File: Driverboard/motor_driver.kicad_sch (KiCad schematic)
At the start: 21 parts

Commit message: WIP
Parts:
- removed R?: 47, symbol Device:R_Small
- R?: value 68 -> 39k
- R?: value 330 -> 27k
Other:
- note added: "The peak current of the motor is 9.5A and the peak phase current of the driver is 8A. The motor have 3 phases and at least two of them active at once. This means that the approximate minimum peak phase current needed for efficient control is: Ioutx = 9.5A / sqrt(3) ~ 5.48A. Therefore if cycle-by-cycle threshold is set to 6A > Ioutx it will be sufficient for the driver to handle the motor load. Th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"
- note added: "~1.35V"
- note removed: "1.25V ILIM gives 8A peak current limit."
- note removed: "~1.24V"
- moved on the sheet: C?, C_AVDD1, C_CP, C_FLY, C_VM1, C_VM2, IC?, L?, R?

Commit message: Powerboard v0.1, not ready for manufacturing yet
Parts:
- removed L? (x2): ?, symbol Device:L_Small
- R?: value 39k -> 27k
- R?: value 27k -> 20k
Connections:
- net GNDREF is gone; now on net GND: C?.2, C?.2, C_AVDD1.2, C_VM1.2, C_VM2.2, IC?.12 (PGND_1), IC?.15 (PGND_2), IC?.18 (PGND_3), IC?.2 (AGND_1), IC?.26 (AGND_2), IC?.4 (GND_BK), IC?.41 (EP), J?.8 (Pin_8), R?.2
- net VM is gone; now on net VCC: C_CP.2, C_VM1.1, C_VM2.1, IC?.10 (VM_2), IC?.11 (VM_3), IC?.9 (VM_1)
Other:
- note added: "The peak current of the motor is 9.5A and the peak phase current of the driver is 8A. The motor have 3 phases and at least two of them active at once. This means that the approximate minimum peak phase current needed for efficient control is: Ioutx = 9.5A / sqrt(3) ~ 5.48A. Therefore if cycle-by-cycle threshold is set to 5.48A*0.9 > Ilim it will be sufficient for the driver to handle the motor lo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"
- note added: "~1.40V"
- note removed: "The peak current of the motor is 9.5A and the peak phase current of the driver is 8A. The motor have 3 phases and at least two of them active at once. This means that the approximate minimum peak phase current needed for efficient control is: Ioutx = 9.5A / sqrt(3) ~ 5.48A. Therefore if cycle-by-cycle threshold is set to 6A > Ioutx it will be sufficient for the driver to handle the motor load. Th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"
- note removed: "~1.35V"

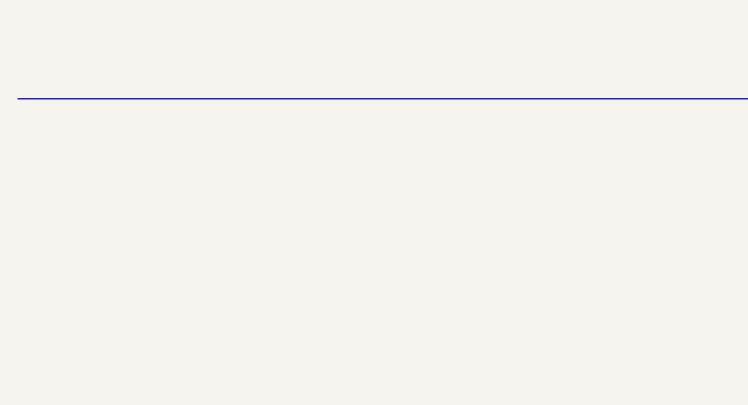
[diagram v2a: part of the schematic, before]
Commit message: DriverboardComp is the complete design, need to be evaluated
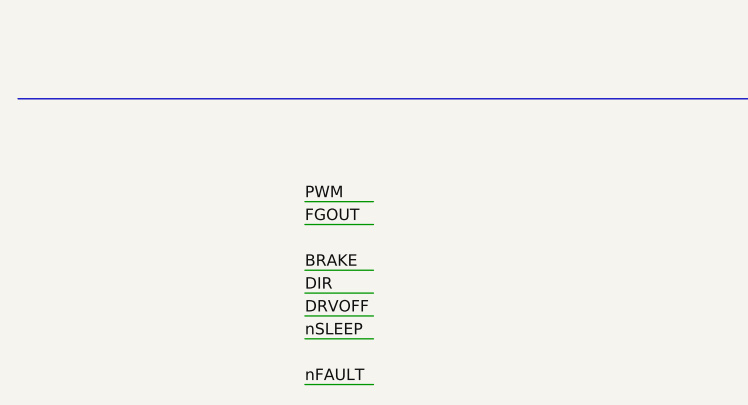
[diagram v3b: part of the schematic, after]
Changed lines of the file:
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@@
+    (stroke (width 0) (type default))
+  )
+  (wire (pts (xy 43.18 149.86) (xy 50.8 149.86))
     (stroke (width 0) (type default))
   )
@@
     (stroke (width 0) (type default))
   )
+  (wire (pts (xy 43.18 154.94) (xy 50.8 154.94))
+    (stroke (width 0) (type default))
+  )
   (wire (pts (xy 143.51 38.735) (xy 151.13 38.735))
     (stroke (width 0) (type default))
@@
     (stroke (width 0) (type default))
   )
+  (wire (pts (xy 43.18 144.78) (xy 50.8 144.78))
+    (stroke (width 0) (type default))
+  )
   (wire (pts (xy 32.512 43.18) (xy 40.64 43.18))
     (stroke (width 0) (type default))
@@
     (stroke (width 0) (type default))
   )
+  (wire (pts (xy 43.18 134.62) (xy 50.8 134.62))
+    (stroke (width 0) (type default))
+  )
   (wire (pts (xy 115.57 52.705) (xy 118.11 52.705))
     (stroke (width 0) (type default))
@@
     (stroke (width 0) (type default))
   )
+  (wire (pts (xy 43.18 142.24) (xy 50.8 142.24))
+    (stroke (width 0) (type default))
+  )
   (wire (pts (xy 85.09 80.645) (xy 118.11 80.645))
     (stroke (width 0) (type default))
@@
     (stroke (width 0) (type default))
   )
+  (wire (pts (xy 43.18 137.16) (xy 50.8 137.16))
+    (stroke (width 0) (type default))
+  )
   (wire (pts (xy 110.49 103.505) (xy 110.49 93.345))
     (stroke (width 0) (type default))
@@
   )
   (wire (pts (xy 161.29 67.945) (xy 173.99 67.945))
+    (stroke (width 0) (type default))
+  )
+  (wire (pts (xy 43.18 147.32) (xy 50.8 147.32))
     (stroke (width 0) (type default))
   )
@@
     (effects (font (size 1.27 1.27)) (justify left bottom))
   )
+  (label "BRAKE" (at 43.18 142.24 0) (fields_autoplaced)
+    (effects (font (size 1.27 1.27)) (justify left bottom))
+  )
   (label "PWM" (at 85.09 85.725 0) (fields_autoplaced)
     (effects (font (size 1.27 1.27)) (justify left bottom))
@@
     (effects (font (size 1.27 1.27)) (justify left bottom))
   )
+  (label "DIR" (at 43.18 144.78 0) (fields_autoplaced)
+    (effects (font (size 1.27 1.27)) (justify left bottom))
+  )
   (label "AVDD" (at 165.1 52.705 0) (fields_autoplaced)
     (effects (font (size 1.27 1.27)) (justify left bottom))
@@
     (effects (font (size 1.27 1.27)) (justify left bottom))
   )
+  (label "PWM" (at 43.18 134.62 0) (fields_autoplaced)
+    (effects (font (size 1.27 1.27)) (justify left bottom))
+  )
   (label "PWM" (at 32.512 66.04 0) (fields_autoplaced)
     (effects (font (size 1.27 1.27)) (justify left bottom))
   )
+  (label "DRVOFF" (at 43.18 147.32 0) (fields_autoplaced)
+    (effects (font (size 1.27 1.27)) (justify left bottom))
+  )
   (label "H3" (at 154.94 86.995 180) (fields_autoplaced)
     (effects (font (size 1.27 1.27)) (justify right bottom))
@@
     (effects (font (size 1.27 1.27)) (justify right bottom))
   )
+  (label "nSLEEP" (at 43.18 149.86 0) (fields_autoplaced)
+    (effects (font (size 1.27 1.27)) (justify left bottom))
+  )
+  (label "FGOUT" (at 43.18 137.16 0) (fields_autoplaced)
+    (effects (font (size 1.27 1.27)) (justify left bottom))
+  )
   (label "V" (at 32.512 35.56 0) (fields_autoplaced)
     (effects (font (size 1.27 1.27)) (justify left bottom))
@@
     (effects (font (size 1.27 1.27)) (justify left bottom))
   )
+  (label "nFAULT" (at 43.18 154.94 0) (fields_autoplaced)
+    (effects (font (size 1.27 1.27)) (justify left bottom))
+  )
